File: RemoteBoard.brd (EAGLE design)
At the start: 50.2 x 56.2 mm, 29 parts, among them J1 SOCKETS9111, J2 SOCKETS9111, J3 SOCKETS9111, J4 CONN_42.54_SCREW, Q3 DMG3404, U1 SPG30, U2 TXS0102DCU, U3 MIC53651.8SC70, U4 BME280, U5 LTC2054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

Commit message: Minor updates to Primary and Remote
Cleaned up/added silkscreen, added test points to both boards
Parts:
- added C12: 1uF, bschulz_passives:C0805
- added TP1, TP2, TP3, TP4, TP5, TP6: TESTPOINTRCU, bschulz:TESTPOINT_0603
- added U8: TCS3400, bschulz:TCS3400
- C9: device bschulz:C0805 -> bschulz_passives:C0805
- J1, J2, J3: value SOCKETS9111 -> SOCKETS9111_SLOT; device bschulz:SOCKET_S9111-45R -> bschulz:SOCKET_S9111-45R_SLOT
- R1, R2, R3, R4: device bschulz:R0805 -> bschulz_passives:R0805
- moved C7 0.38 mm to (16.9, 45.2)
- moved C8 0.38 mm to (24.0, 48.5)
- moved C9 0.38 mm to (13.1, 42.5)
- moved R1 0.38 mm to (26.9, 45.2)
- moved R2 0.38 mm to (29.2, 45.2)
- moved R3 0.38 mm to (21.2, 45.2)
- moved R4 0.38 mm to (19.1, 45.2)
- moved U5 0.38 mm to (24.0, 45.2)
- moved U6 0.38 mm to (13.1, 45.2)
- moved J1 0.13 mm to (39.4, 45.5)
- moved J2 0.13 mm to (39.4, 32.0)
- moved J3 0.13 mm to (46.1, 38.7)
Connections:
- removed net N$2: R3.2, R4.1, U5.1
- removed net N$3: C7.1, R4.2, U6.3
- new net O2_GAIN: R3.2, R4.1, TP4.1, U5.1
- new net O2_LPF: C7.1, R4.2, TP1.1, U6.3
- net 3V3: now also C12.1, U8.1
- net GND: now also C12.2, TP3.1, U8.3, U8.4
- net O2+: now also TP2.1
- net SCL: now also TP5.1, U8.2
- net SDA: now also TP6.1, U8.6
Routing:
- net SCL: track 80.9 -> 94.5 mm
- net SDA: track 75.3 -> 88.5 mm, vias 4 -> 5
- net O2_LPF: track 0.00 -> 6.59 mm
- net O2_GAIN: track 0.00 -> 6.39 mm
- net 3V3: track 107.2 -> 112.2 mm
- net N$3: track 4.62 -> 0.00 mm
- net N$2: track 4.17 -> 0.00 mm
- net O2+: track 16.2 -> 19.5 mm
- net GND: track 154.7 -> 156.2 mm, vias 4 -> 5
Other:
- board text added: "No Cover!"
- board text added: "Project-Palmer v0.0 Bobby Schulz"
- board text added: "SCL"
- board text added: "SDA"
- board text added: "To Logger 3.3v"
- board text added: "V+"
- board text added: "V-"

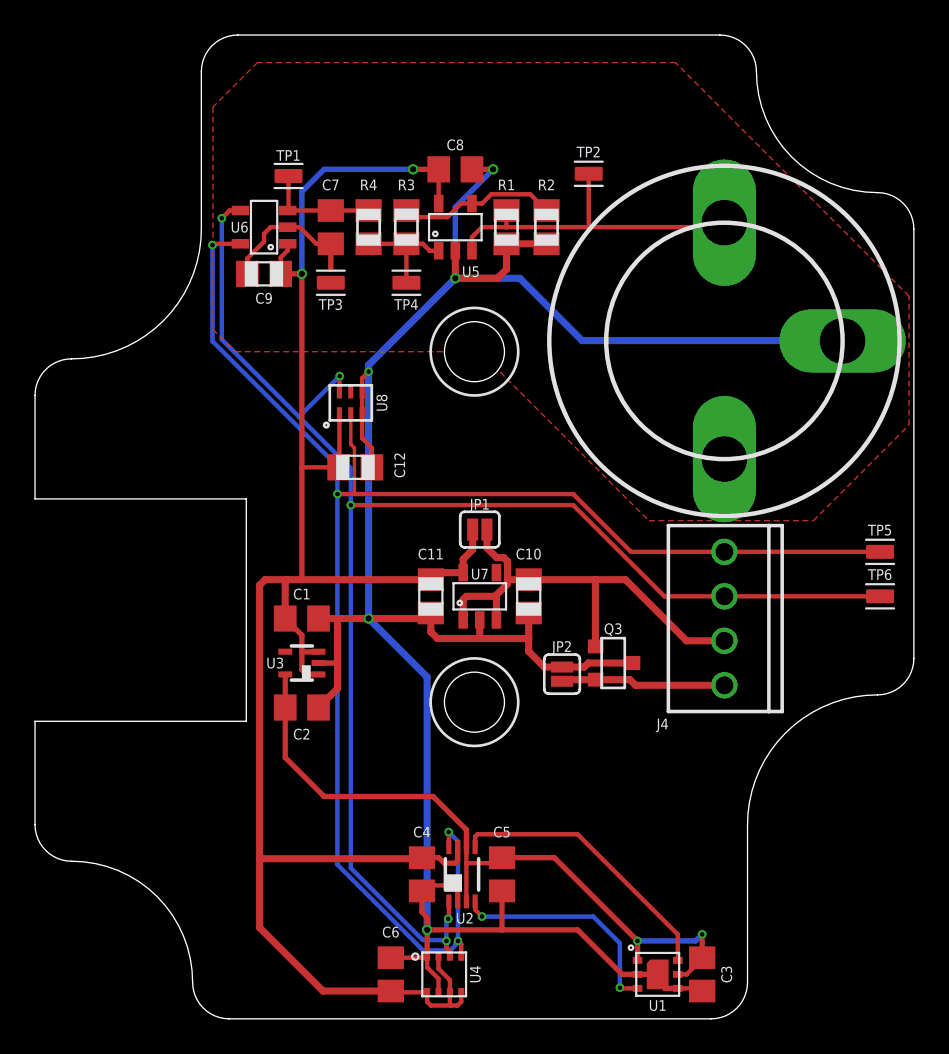
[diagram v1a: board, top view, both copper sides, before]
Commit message: Minor cleanup/fixes to boards, generated gerbers
Minor changes to boards, primarily cleanup and generated gerbers for fab, ready for review
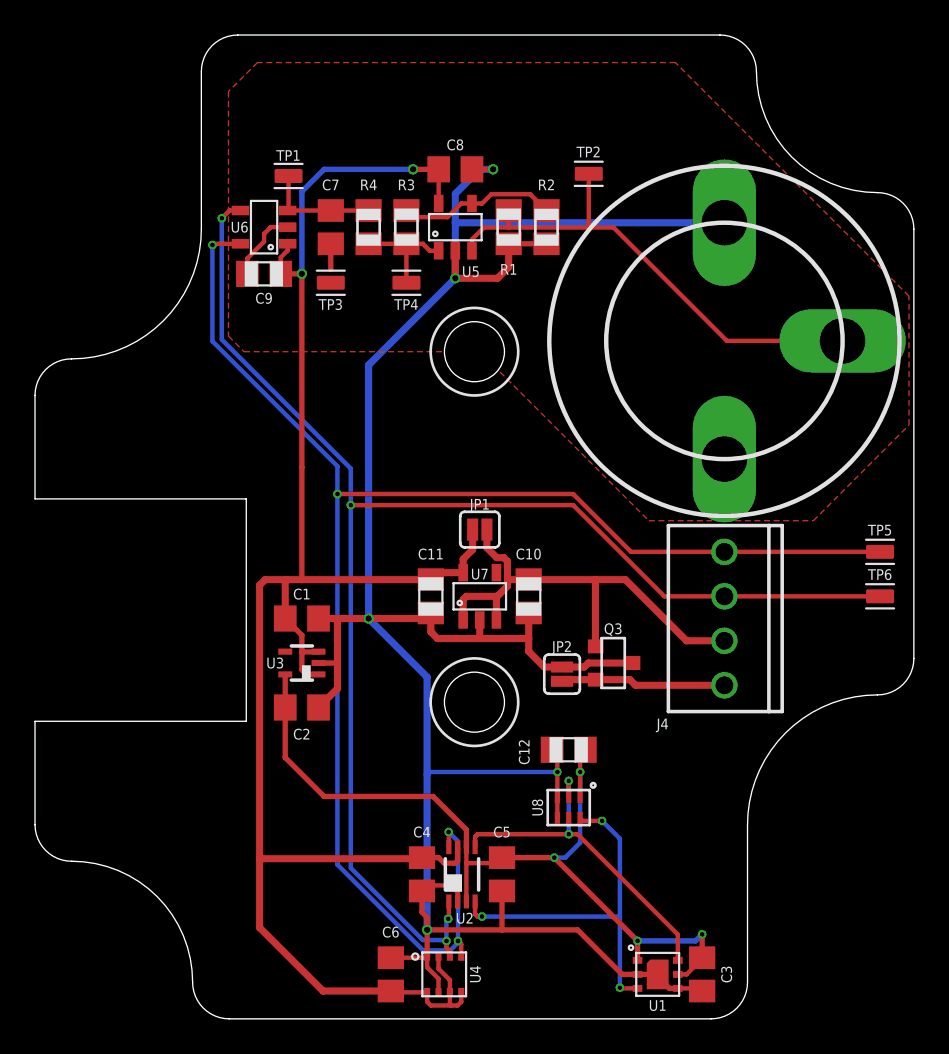
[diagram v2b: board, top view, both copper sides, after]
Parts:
- R2: value (none) -> 1k
- R3: value (none) -> 78.7k
- moved U8 26.3 mm to (30.5, 12.1), turned to 270 degrees
- moved C12 20.2 mm to (30.5, 15.4), turned to 180 degrees
- moved R1 0.13 mm to (27.1, 45.2), turned to 270 degrees
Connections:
- net 1V8: now also C12.1, U8.1
- net 3V3: no longer C12.1, U8.1
- net GND: now also J1.PAD, R1.2; no longer J3.PAD, R1.1
- net O2+: now also J3.PAD, R1.1; no longer J1.PAD, R1.2
- net SCL: no longer U8.2
- net SCL_LV: now also U8.2
- net SDA: no longer U8.6
- net SDA_LV: now also U8.6
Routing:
- net O2+: track 19.5 -> 28.8 mm
- net 1V8: track 40.9 -> 49.6 mm, vias 2 -> 4
- net SDA_LV: track 13.1 -> 21.3 mm, vias 2 -> 3
- net 3V3: track 112.2 -> 107.0 mm
- net GND: track 156.2 -> 151.0 mm
- net SCL: track 94.5 -> 89.8 mm
- net SDA: track 88.5 -> 84.3 mm, vias 5 -> 4
- net SCL_LV: track 16.1 -> 20.0 mm, vias 0 -> 2
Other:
- board text added: "Project-Palmer Remote v0.0 Bobby Schulz"
- board text removed: "Project-Palmer v0.0 Bobby Schulz"

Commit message: Minor updates, part vals
Changed 1x7 connector on Primary board to 1x4 and 1x3 because 1x7 0.1" screw terminals are made of Corinthian Leather apparently, also updated part values and BoM vals
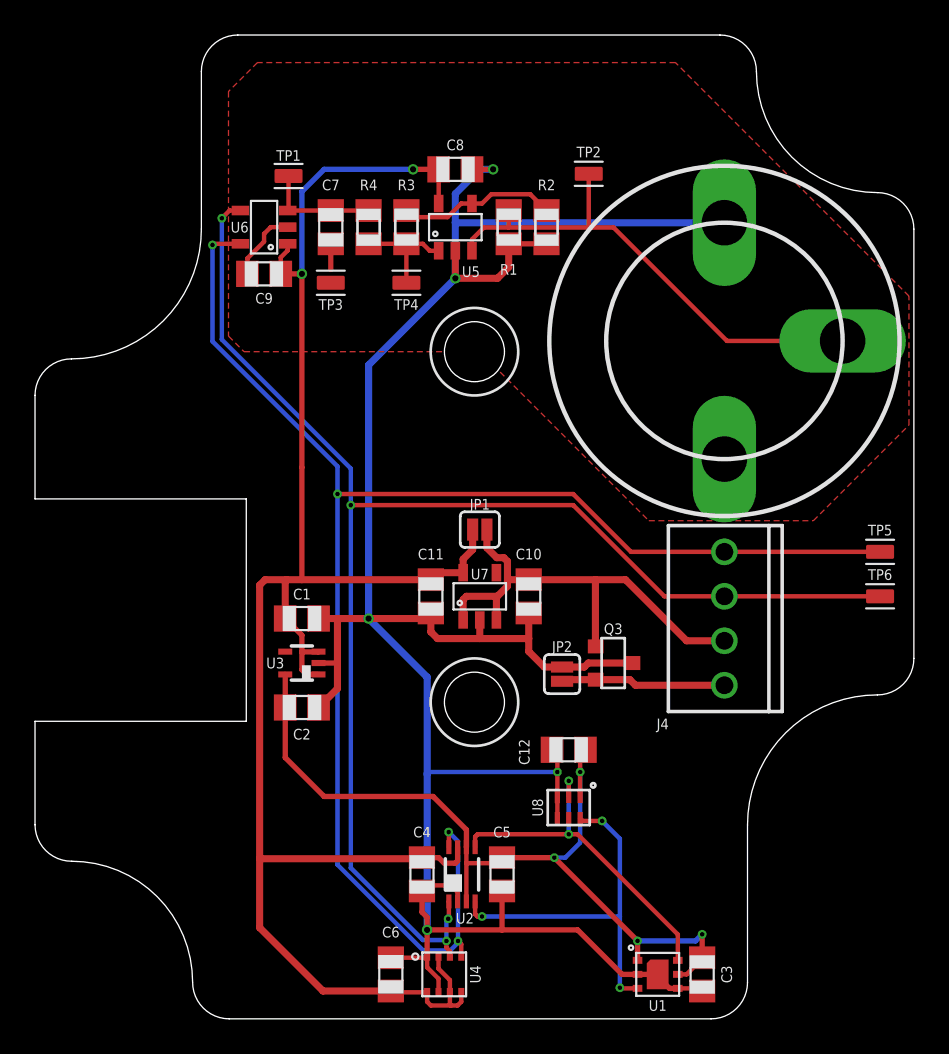
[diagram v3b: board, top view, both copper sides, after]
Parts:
- C1, C2, C6, C7, C8: device bschulz:C0805 -> bschulz_passives:C0805
- C3, C4, C5: value (none) -> 0.1uF; device bschulz:C0805 -> bschulz_passives:C0805
